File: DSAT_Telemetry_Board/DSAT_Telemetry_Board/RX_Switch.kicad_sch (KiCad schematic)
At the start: 5 parts

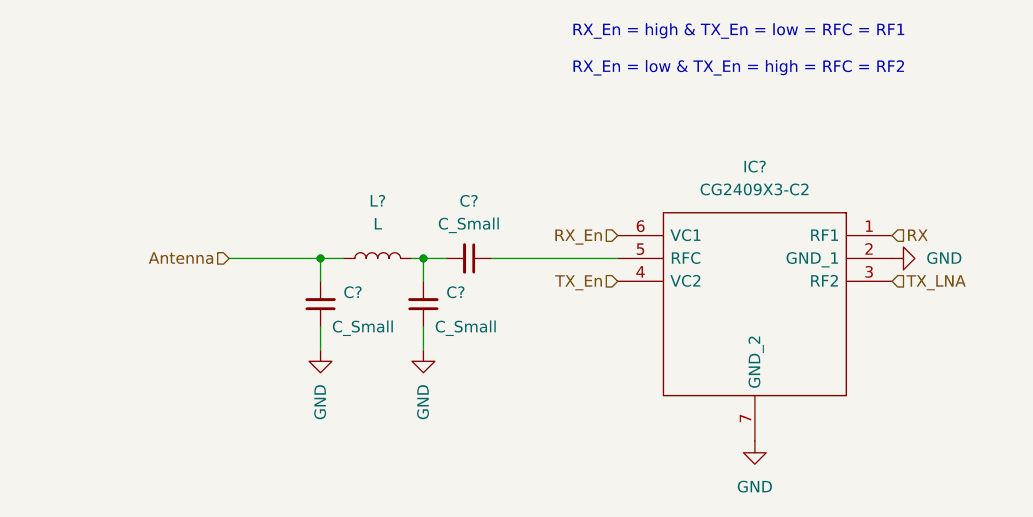
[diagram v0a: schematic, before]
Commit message: Added Matching Networks/Linear Regulator/Watchdog Pins
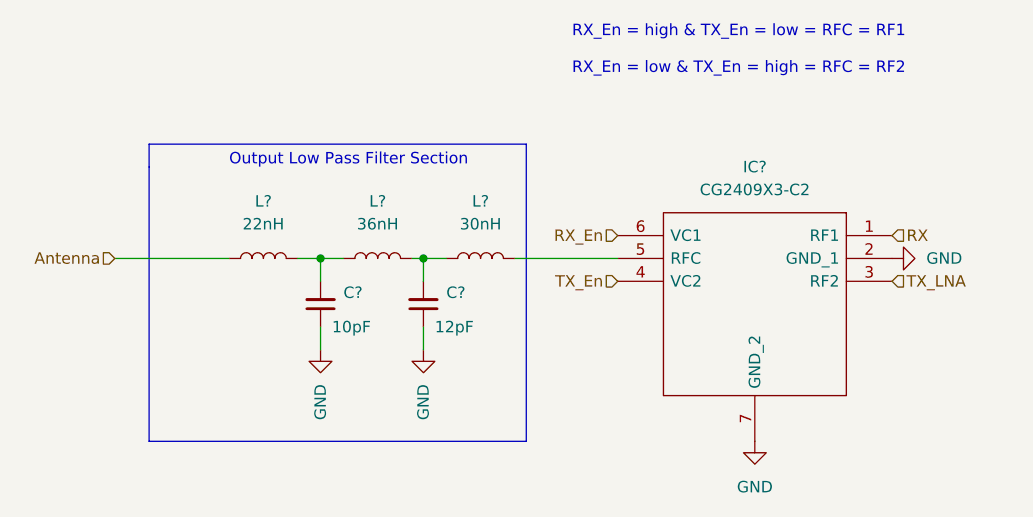
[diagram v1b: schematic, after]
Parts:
- removed C?: C_Small, symbol Device:C_Small
- added L?: 30nH, symbol Device:L
- added L?: 22nH, symbol Device:L
- C?: value C_Small -> 12pF
- C?: value C_Small -> 10pF
- L?: value L -> 36nH
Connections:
- net Antenna: now also L?.1; no longer C?.2, L?.1
- net at C?.2, L?.2: now also L?.1
- net at IC?.5 (RFC): now also L?.2
- new net: C?.2, L?.1, L?.2
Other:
- note added: "Output Low Pass Filter Section"
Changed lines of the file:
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@@
   (junction (at 97.79 93.98) (diameter 0) (color 0 0 0 0)
   )
+  (wire (pts (xy 95.25 93.98) (xy 97.79 93.98))
+    (stroke (width 0) (type default) (color 0 0 0 0))
+  )
   (wire (pts (xy 109.22 93.98) (xy 111.76 93.98))
     (stroke (width 0) (type default) (color 0 0 0 0))
@@
     (stroke (width 0) (type default) (color 0 0 0 0))
   )
+  (polyline (pts (xy 120.65 81.28) (xy 78.74 81.28))
+    (stroke (width 0) (type default) (color 0 0 0 0))
+  )
   (wire (pts (xy 107.95 93.98) (xy 109.22 93.98))
     (stroke (width 0) (type default) (color 0 0 0 0))
@@
     (stroke (width 0) (type default) (color 0 0 0 0))
   )
-  (wire (pts (xy 116.84 93.98) (xy 130.81 93.98))
-    (stroke (width 0) (type default) (color 0 0 0 0))
-  )
   (wire (pts (xy 109.22 101.6) (xy 109.22 104.14))
     (stroke (width 0) (type default) (color 0 0 0 0))
   )
-  (wire (pts (xy 87.63 93.98) (xy 97.79 93.98))
+  (polyline (pts (xy 78.74 114.3) (xy 120.65 114.3))
+    (stroke (width 0) (type default) (color 0 0 0 0))
+  )
+  (polyline (pts (xy 78.74 81.28) (xy 78.74 83.82))
+    (stroke (width 0) (type default) (color 0 0 0 0))
+  )
+  (polyline (pts (xy 120.65 114.3) (xy 120.65 81.28))
     (stroke (width 0) (type default) (color 0 0 0 0))
   )
@@
     (stroke (width 0) (type default) (color 0 0 0 0))
   )
+  (wire (pts (xy 119.38 93.98) (xy 130.81 93.98))
+    (stroke (width 0) (type default) (color 0 0 0 0))
+  )
   (wire (pts (xy 109.22 93.98) (xy 109.22 96.52))
+    (stroke (width 0) (type default) (color 0 0 0 0))
+  )
+  (polyline (pts (xy 78.74 83.82) (xy 78.74 114.3))
+    (stroke (width 0) (type default) (color 0 0 0 0))
+  )
+  (wire (pts (xy 74.93 93.98) (xy 87.63 93.98))
     (stroke (width 0) (type default) (color 0 0 0 0))
   )
@@
     (effects (font (size 1.27 1.27)) (justify left bottom))
   )
+  (text "Output Low Pass Filter Section" (at 87.63 83.82 0)
+    (effects (font (size 1.27 1.27)) (justify left bottom))
+  )
   (hierarchical_label "RX_En" (shape input) (at 130.81 91.44 180)
     (effects (font (size 1.27 1.27)) (justify right))
@@
     (effects (font (size 1.27 1.27)) (justify right))
   )
-  (hierarchical_label "Antenna" (shape input) (at 87.63 93.98 180)
+  (hierarchical_label "Antenna" (shape input) (at 74.93 93.98 180)
     (effects (font (size 1.27 1.27)) (justify right))
   )
@@
   (hierarchical_label "TX_LNA" (shape input) (at 161.29 96.52 0)
     (effects (font (size 1.27 1.27)) (justify left))
+  )
+  (symbol (lib_id "Device:L") (at 115.57 93.98 90) (unit 1)
+    (in_bom yes) (on_board yes) (fields_autoplaced)
+    (property "Reference" "L?" (id 0) (at 115.57 87.63 90))
+    (property "Value" "30nH" (id 1) (at 115.57 90.17 90))
+    (property "Footprint" "" (id 2) (at 115.57 93.98 0)
+      (effects (font (size 1.27 1.27)) hide)
+    )
+    (property "Datasheet" "~" (id 3) (at 115.57 93.98 0)
+      (effects (font (size 1.27 1.27)) hide)
+    )
+    (pin "1")
+    (pin "2")
+  )
+  (symbol (lib_id "Device:L") (at 91.44 93.98 90) (unit 1)
+    (in_bom yes) (on_board yes) (fields_autoplaced)
+    (property "Reference" "L?" (id 0) (at 91.44 87.63 90))
+    (property "Value" "22nH" (id 1) (at 91.44 90.17 90))
+    (property "Footprint" "" (id 2) (at 91.44 93.98 0)
+      (effects (font (size 1.27 1.27)) hide)
+    )
+    (property "Datasheet" "~" (id 3) (at 91.44 93.98 0)
+      (effects (font (size 1.27 1.27)) hide)
+    )
+    (pin "1")
+    (pin "2")
   )
   (symbol (lib_id "power:GND") (at 161.29 93.98 90) (mirror x) (unit 1)
@@
       (effects (font (size 1.27 1.27)) (justify right))
     )
-    (property "Value" "C_Small" (id 1) (at 110.49 101.6 0)
+    (property "Value" "12pF" (id 1) (at 110.49 101.6 0)
       (effects (font (size 1.27 1.27)) (justify right))
     )
@@
     (in_bom yes) (on_board yes) (fields_autoplaced)
     (property "Reference" "L?" (id 0) (at 104.14 87.63 90))
-    (property "Value" "L" (id 1) (at 104.14 90.17 90))
+    (property "Value" "36nH" (id 1) (at 104.14 90.17 90))
     (property "Footprint" "" (id 2) (at 104.14 93.98 0)
       (effects (font (size 1.27 1.27)) hide)
@@
     (pin "7")
   )
-  (symbol (lib_id "Device:C_Small") (at 114.3 93.98 270) (mirror x) (unit 1)
-    (in_bom yes) (on_board yes) (fields_autoplaced)
-    (property "Reference" "C?" (id 0) (at 114.2936 87.63 90))
-    (property "Value" "C_Small" (id 1) (at 114.2936 90.17 90))
-    (property "Footprint" "" (id 2) (at 114.3 93.98 0)
-      (effects (font (size 1.27 1.27)) hide)
-    )
-    (property "Datasheet" "~" (id 3) (at 114.3 93.98 0)
-      (effects (font (size 1.27 1.27)) hide)
-    )
-    (pin "1")
-    (pin "2")
-  )
   (symbol (lib_id "Device:C_Small") (at 97.79 99.06 180) (unit 1)
     (in_bom yes) (on_board yes)
@@
       (effects (font (size 1.27 1.27)) (justify right))
     )
-    (property "Value" "C_Small" (id 1) (at 99.06 101.6 0)
-      (effects (font (size 1.27 1.27)) (justify right))
-    )
+    (property "Value" "10pF" (id 1) (at 99.06 101.6 0)
+      (effects (font (size 1.27 1.27)) (justify right))
+    )
